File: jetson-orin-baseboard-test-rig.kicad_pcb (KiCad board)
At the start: 2 copper layers, 150 x 150 mm, 229 parts, among them J1 PinHeader_2x6_P2.54mm_Drill1.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, J10 Harwin_1x1_H17.75mm_Drill0.8m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, J11 Harwin_1x1_H17.75mm_Drill0.8m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, J12 Harwin_1x1_H17.75mm_Drill0.8m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, J13 Harwin_1x1_H17.75mm_Drill0.8m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, J14 Harwin_1x1_H17.75mm_Drill0.8m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, J15 Harwin_1x1_H17.75mm_Drill0.8m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, J16 Harwin_1x1_H17.75mm_Drill0.8m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, J17 Harwin_1x1_H17.75mm_Drill0.8m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, J18 Harwin_1x1_H17.75mm_Drill0.8m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, J19 Harwin_1x1_H17.75mm_Drill0.8m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, J2 PinHeader_2x6_P2.54mm_Drill1.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, J20 Harwin_1x1_H17.75mm_Drill0.8m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, J21 Harwin_1x1_H17.75mm_Drill0.8m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, J22 Harwin_1x1_H17.75mm_Drill0.8m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, J23 Harwin_1x1_H17.75mm_Drill0.8m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, J24 Harwin_1x1_H17.75mm_Drill0.8m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, J25 Harwin_1x1_H17.75mm_Drill0.8m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, J26 Harwin_1x1_H17.75mm_Drill0.8m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, J27 Harwin_1x1_H17.75mm_Drill0.8m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, J28 Harwin_1x1_H17.75mm_Drill0.8m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, J29 Harwin_1x1_H17.75mm_Drill0.8m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, J3 PinHeader_2x6_P2.54mm_Drill1.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, J30 Harwin_1x1_H17.75mm_Drill0.8m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, J4 PinHeader_2x6_P2.54mm_Drill1.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, J5 PinHeader_2x6_P2.54mm_Drill1.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, J6 PinHeader_2x6_P2.54mm_Drill1.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, J7 PinHeader_2x6_P2.54mm_Drill1.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, J8 Harwin_1x1_H17.75mm_Drill0.8m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, J9 Harwin_1x1_H17.75mm_Drill0.8m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, Q1 BSS84

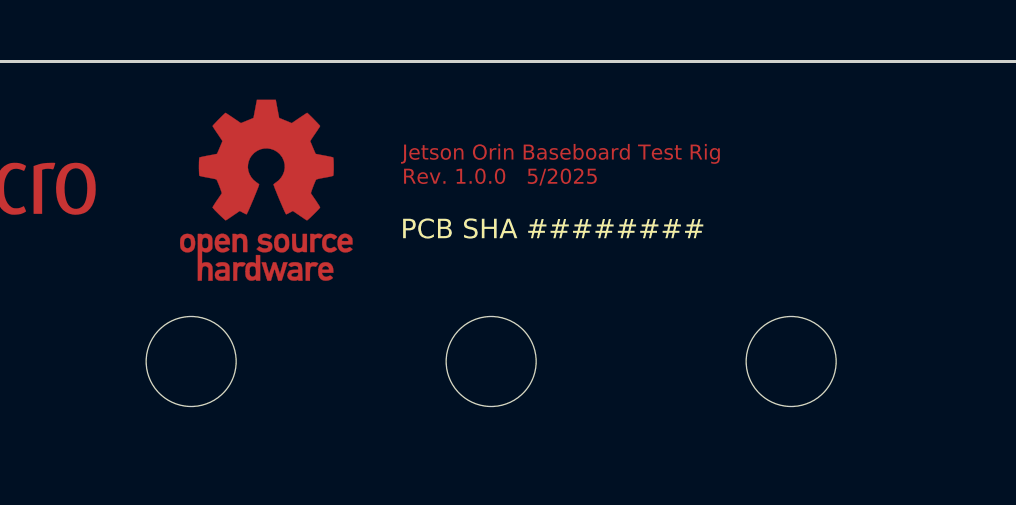
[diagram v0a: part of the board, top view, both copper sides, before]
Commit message: [#77400] Update date, update logos
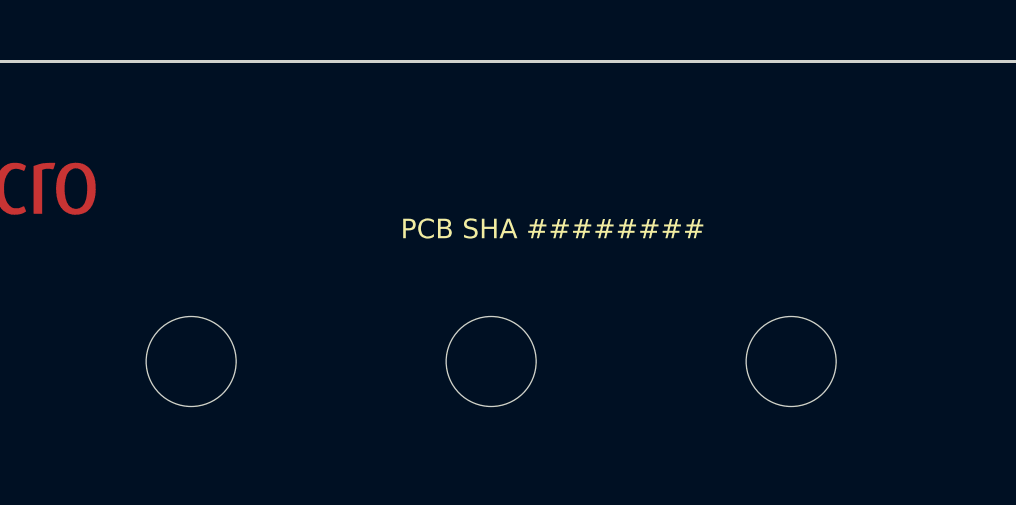
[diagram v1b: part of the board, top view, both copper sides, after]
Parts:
- removed the REF** at (172.5, 54.3)
